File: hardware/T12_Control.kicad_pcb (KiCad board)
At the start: 2 copper layers, 33 parts, among them J1 Screw_Terminal_01x02, J3 Conn_01x07_Female, J4 Conn_01x04_Female, J5 Conn_01x06_Male, J6 Conn_01x04_Male, Q1 TPC8107, Q2 SI2308A, U1 LF15_TO252, U2 24LC32, U3 SGM8551XN, U4 STM32F103CBTx

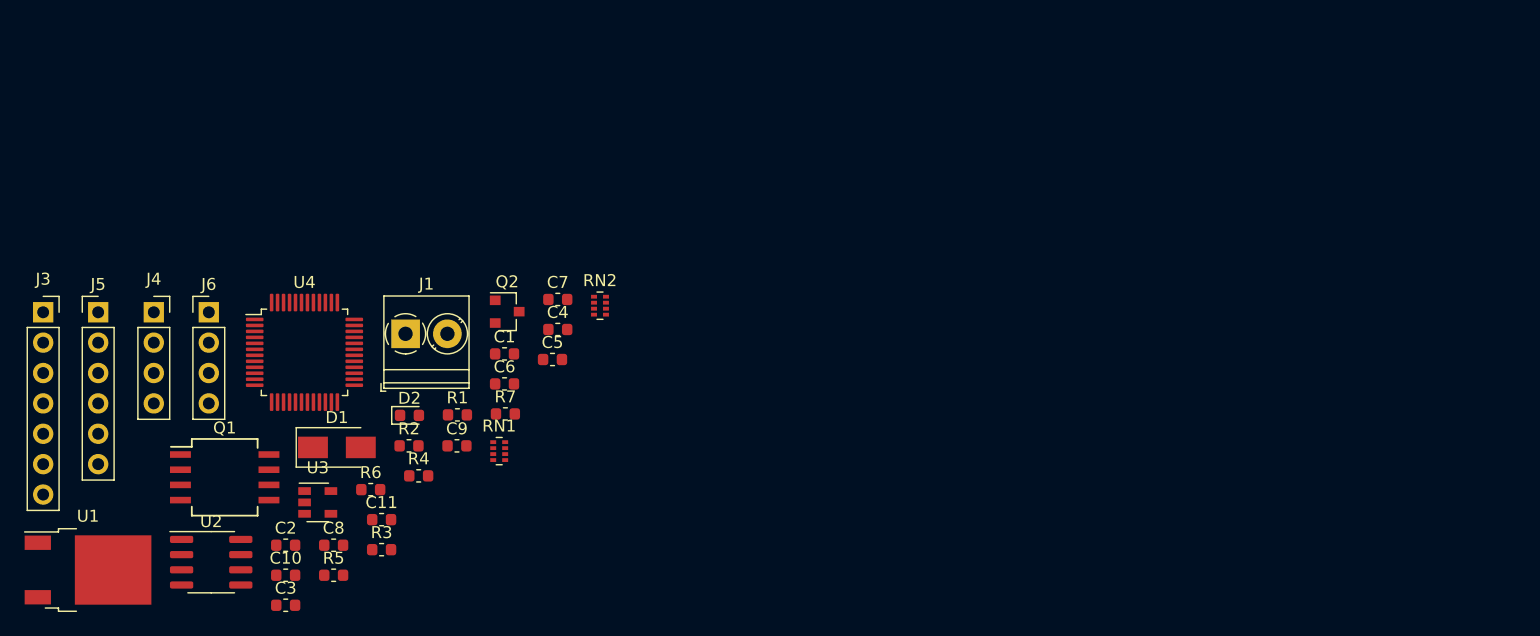
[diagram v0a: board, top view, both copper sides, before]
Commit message: Routhe the T12 Iron controller.
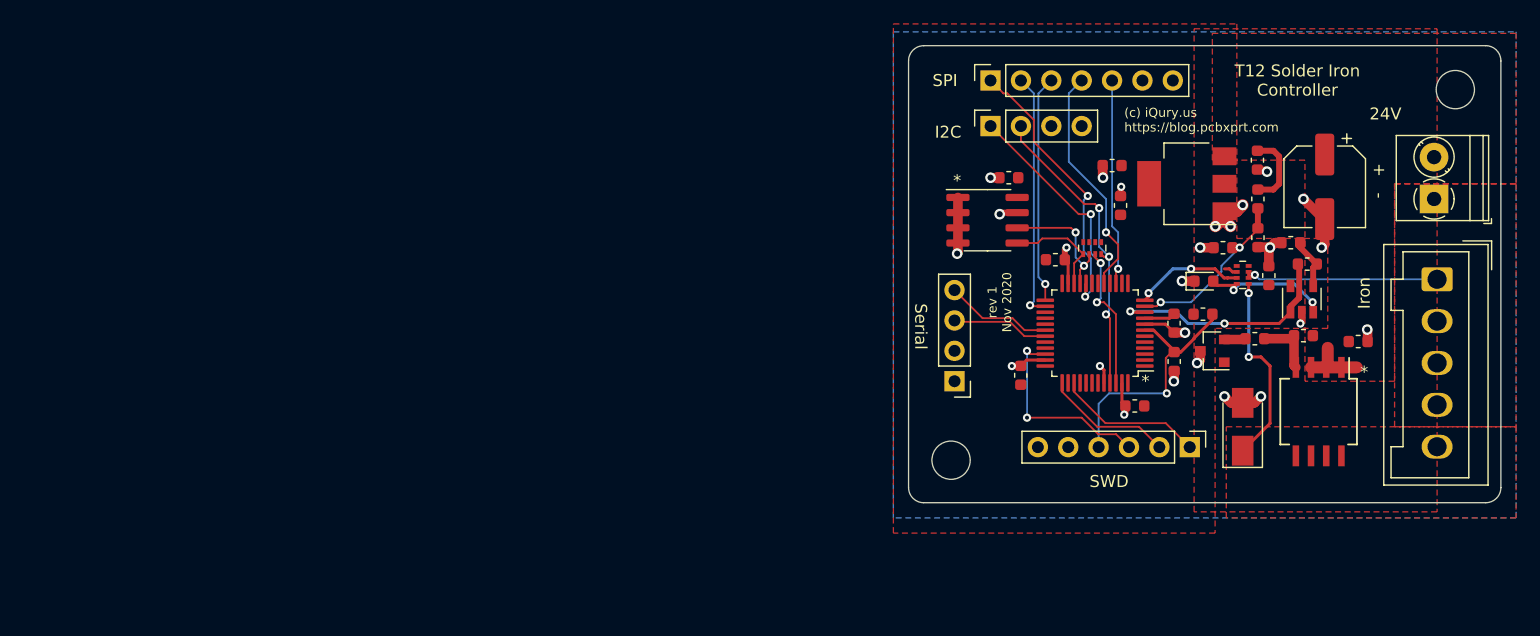
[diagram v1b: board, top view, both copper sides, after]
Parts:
- added C12: 100uF 35V, Capacitor_SMD:CP_Elec_6.3x7.7, F.Cu at (230.4, 82.8)
- added C13: 100nF, Capacitor_SMD:C_0603_1608Metric, F.Cu at (225.7, 90.2)
- added H1: MountingHole, MountingHole:MountingHole_3.2mm_M3_DIN965, F.Cu at (199.1, 105.7)
- added H2: MountingHole, MountingHole:MountingHole_3.2mm_M3_DIN965, F.Cu at (241.3, 74.7)
- added J2: GX12-5M, Connector_Wago:Wago_734-135_1x05_P3.50mm_Vertical, F.Cu at (239.8, 90.5)
- J3: value Conn_01x07_Female -> SPI LCD
- J4: value Conn_01x04_Female -> I2C LCD
- J5: value Conn_01x06_Male -> SWD
- J6: value Conn_01x04_Male -> Serial
- U1: value LF15_TO252 -> AMS1117-3.3; footprint Package_TO_SOT_SMD:TO-252-2 -> Package_TO_SOT_SMD:SOT-223-3_TabPin2
- moved U1 97.4 mm to (218.8, 82.5), turned to 180 degrees
- moved J5 92.0 mm to (219.1, 104.6), turned to -90 degrees
- moved Q1 91.6 mm to (229.9, 101.6), turned to -90 degrees
- moved C2 87.4 mm to (224.8, 80.6), turned to -90 degrees
- moved J1 86.7 mm to (239.5, 83.8), turned to 90 degrees
- moved R5 84.7 mm to (227.5, 87.5), turned to 180 degrees
- moved U3 84.0 mm to (228.5, 92.2), turned to 90 degrees
- moved J3 81.6 mm to (202.4, 73.9), turned to 90 degrees
- moved R6 80.6 mm to (228.9, 89.3), turned to 180 degrees
- moved C3 77.4 mm to (213.3, 84.4), turned to 90 degrees
- moved C10 77.2 mm to (217.8, 94.2), turned to -90 degrees
- moved D1 75.8 mm to (223.5, 102.9), turned to 90 degrees
- moved R3 75.1 mm to (224.5, 95.5), turned to 180 degrees
- moved R2 73.9 mm to (224.8, 83.8), turned to -90 degrees
- moved R4 72.9 mm to (224.8, 87.1), turned to -90 degrees
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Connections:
- Q2 pad 1: /HEARER_ON -> (no net)
- RN1 pad 1: Net-(RN1-Pad1) -> (no net)
- RN1 pad 8: Net-(RN1-Pad8) -> (no net)
- U1 pad 1: /24V -> GND
- U1 pad 2: GND -> /3.3V
- U1 pad 3: /3.3V -> /24V
- U4 pad 13: /ADC2 -> (no net)
- U4 pad 14: Net-(U4-Pad14) -> (no net)
- U4 pad 16: /MISO -> (no net)
- U4 pad 18: /PWM2 -> (no net)
- U4 pad 19: /PWM3 -> (no net)
- U4 pad 2: /IO_1 -> (no net)
- U4 pad 27: Net-(U4-Pad27) -> (no net)
- U4 pad 28: Net-(U4-Pad28) -> (no net)
- U4 pad 29: /HEATER_ON -> (no net)
- U4 pad 3: /IO_2 -> (no net)
- U4 pad 32: Net-(U4-Pad32) -> (no net)
- U4 pad 33: Net-(U4-Pad33) -> (no net)
- U4 pad 38: /PWM1 -> (no net)
- U4 pad 4: /IO_3 -> (no net)
- U4 pad 40: Net-(U4-Pad40) -> (no net)
- U4 pad 41: Net-(U4-Pad41) -> (no net)
- U4 pad 42: Net-(U4-Pad42) -> (no net)
- U4 pad 43: Net-(U4-Pad43) -> (no net)
- U4 pad 5: Net-(U4-Pad5) -> (no net)
- U4 pad 6: Net-(U4-Pad6) -> (no net)
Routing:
- net GND: track 0.00 -> 47.0 mm, vias 0 -> 25
- net /OLED_SDA: track 0.00 -> 28.0 mm, vias 0 -> 3
- net /OLED_SCL: track 0.00 -> 26.1 mm, vias 0 -> 3
- net /~CS: track 0.00 -> 23.4 mm, vias 0 -> 2
- net /~NRST: track 0.00 -> 21.7 mm, vias 0 -> 1
- net /D/~C: track 0.00 -> 20.7 mm, vias 0 -> 1
- net /TIP_TEMP: track 0.00 -> 19.8 mm, vias 0 -> 2
- net /MOSI: track 0.00 -> 19.6 mm, vias 0 -> 1
- net /~RST: track 0.00 -> 19.1 mm, vias 0 -> 1
- net /SCK: track 0.00 -> 17.2 mm, vias 0 -> 1
- net /SWDIO: track 0.00 -> 16.8 mm, vias 0 -> 2
- net Net-(J2-Pad1): track 0.00 -> 16.5 mm, vias 0 -> 1
- net Net-(D1-Pad1): track 0.00 -> 16.2 mm, vias 0 -> 2
- net /V_MON: track 0.00 -> 14.8 mm, vias 0 -> 2
- net /SWDSWO: track 0.00 -> 12.3 mm
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- added copper zone on F.Cu, net /24V
- added copper zone on F.Cu, net /3.3V
- added copper zone on B.Cu, net GND
- added copper zone on F.Cu, net GND
- added copper zone on F.Cu, net Net-(D1-Pad1)
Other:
- board outline added: 49.5 x 38.2 mm
- board text added: "(c) iQury.us https://blog.pcbxprt.com"
- board text added: "*"
- board text added: "+ -"
- board text added: "24V"
- board text added: "3.3V"
- board text added: "D/~C"
- board text added: "GND"
- board text added: "HEATER"
- board text added: "I2C"
- board text added: "Iron"
- board text added: "MOSI"
- board text added: "N/C"
- board text added: "NTC"
- board text added: "RX"
- board text added: "SCK"
- board text added: "SCL"
- board text added: "SDA"
- board text added: "SPI"
- board text added: "SWD"
- board text added: "SWDCLK"
- board text added: "SWDIO"
- board text added: "SWDSWO"
- board text added: "Serial"
- board text added: "T12 Solder Iron Controller"
- board text added: "TX"
- board text added: "rev 1 Nov 2020"
- board text added: "~CS"
- board text added: "~RESET"
- board text added: "~RST"

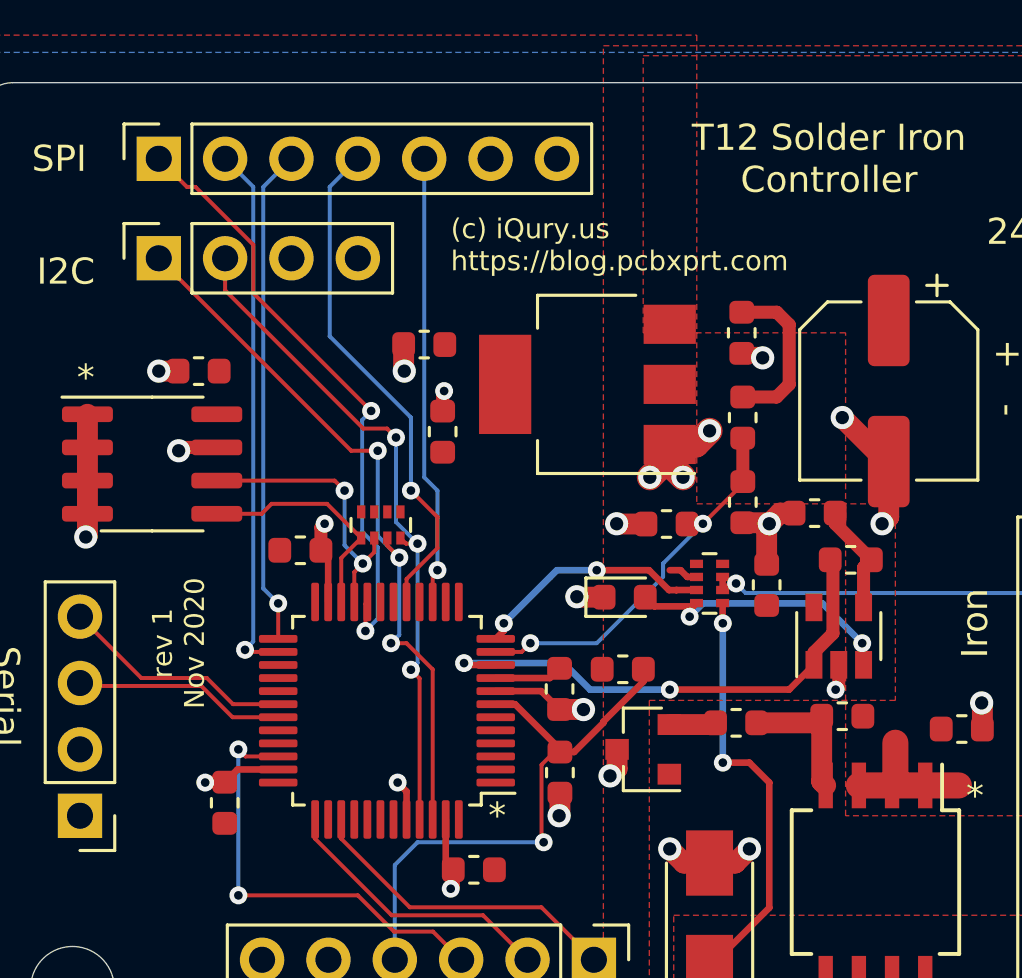
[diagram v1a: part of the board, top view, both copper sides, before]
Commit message: Added LCSC Part #s Generated fab files.
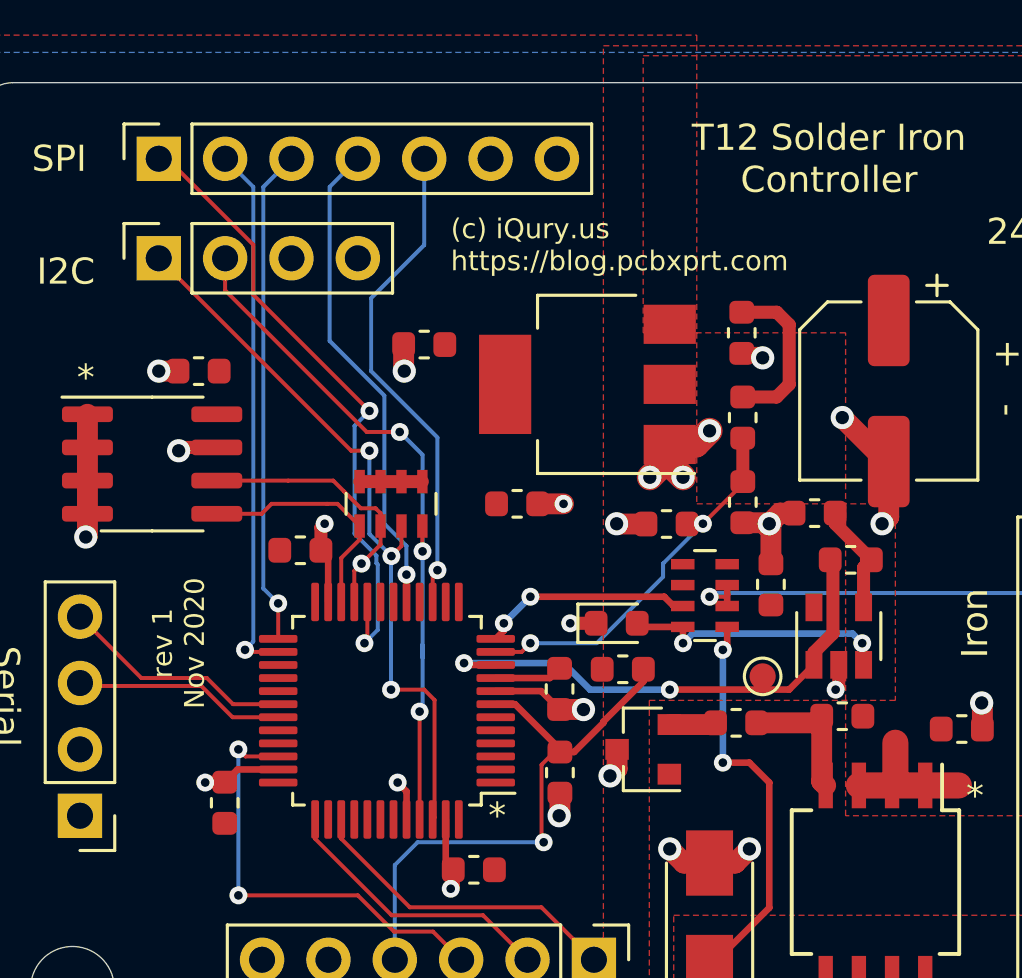
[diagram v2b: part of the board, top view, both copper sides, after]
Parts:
- added TP1: TestPoint, TestPoint:TestPoint_Pad_D1.0mm, F.Cu at (225.6, 93.7)
- C5: value 6.3uF -> 10uF
- RN1, RN2: footprint Resistor_SMD:R_Array_Concave_4x0402 -> Resistor_SMD:R_Array_Concave_4x0603
- moved C3 3.97 mm to (216.2, 87.1), turned to 0 degrees
- moved D2 1.04 mm to (220.0, 91.7)
- moved RN2 0.90 mm to (211.3, 87.1)
- moved RN1 0.49 mm to (223.3, 90.6)
- moved C13 0.16 mm to (225.9, 90.2)
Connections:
- RN1 pad 1: (no net) -> Net-(RN1-Pad1)
- RN1 pad 8: (no net) -> Net-(RN1-Pad8)
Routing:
- net /SCK: track 17.2 -> 18.9 mm
- net Net-(J2-Pad1): track 16.5 -> 17.8 mm
- net /3.3V: track 3.73 -> 5.00 mm
- net /~CS: track 23.4 -> 24.5 mm
- net /NTC: track 9.26 -> 8.14 mm
- net /MOSI: track 19.6 -> 18.6 mm
- net Net-(D1-Pad1): track 16.2 -> 15.4 mm
- net /OLED_SCL: track 26.1 -> 26.9 mm
- net Net-(D2-Pad2): track 11.1 -> 10.4 mm
- net /EE_SCL: track 11.1 -> 10.6 mm, vias 2 -> 1

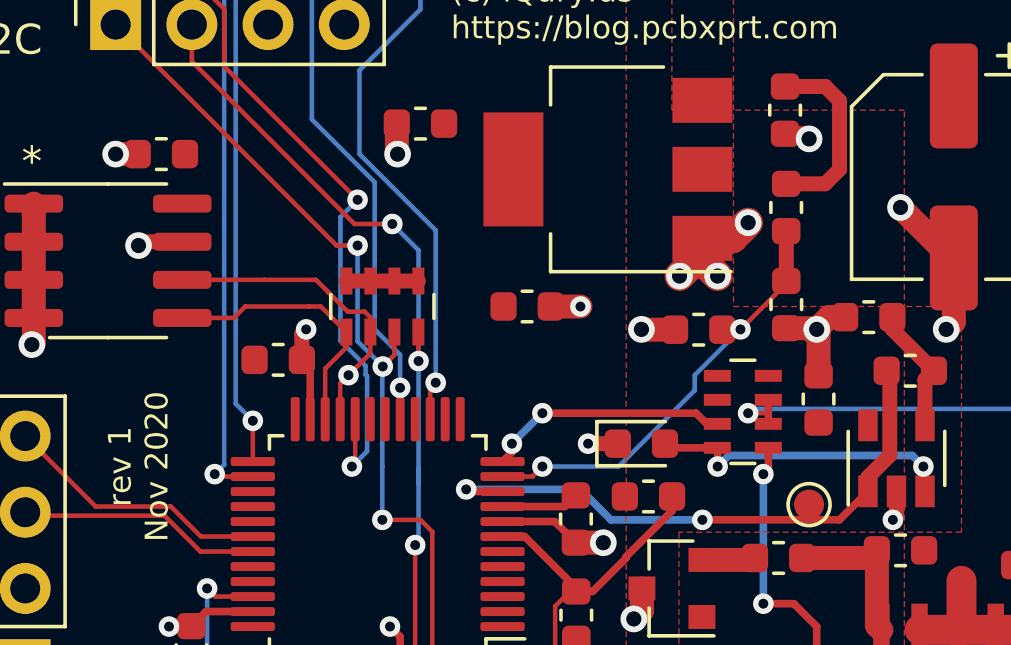
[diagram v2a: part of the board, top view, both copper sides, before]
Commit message: Revert the resistor networks back to 4x0402 footprint, not using JLC assembly svc for now.
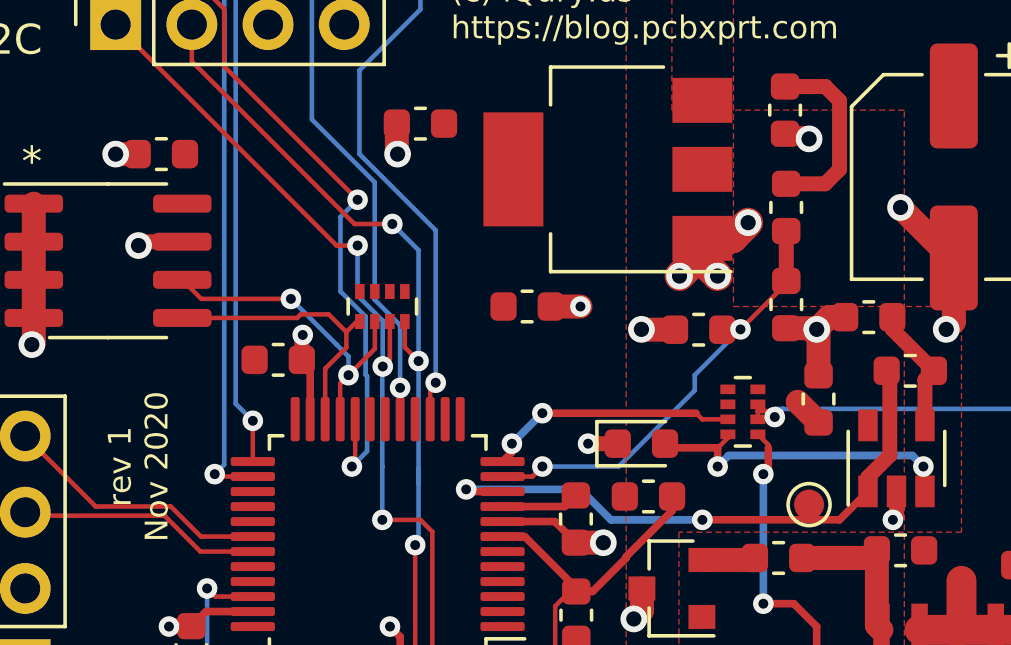
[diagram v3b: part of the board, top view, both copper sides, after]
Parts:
- RN1, RN2: footprint Resistor_SMD:R_Array_Concave_4x0603 -> Resistor_SMD:R_Array_Concave_4x0402
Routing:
- net /3.3V: track 5.00 -> 3.58 mm
- net Net-(J2-Pad1): track 17.8 -> 16.9 mm
- net Net-(D2-Pad2): track 10.4 -> 11.0 mm
- net Net-(D1-Pad1): track 15.4 -> 16.0 mm
- net /OLED_SCL: track 26.9 -> 27.4 mm
- net /EE_SCL: track 10.6 -> 11.0 mm, vias 1 -> 2

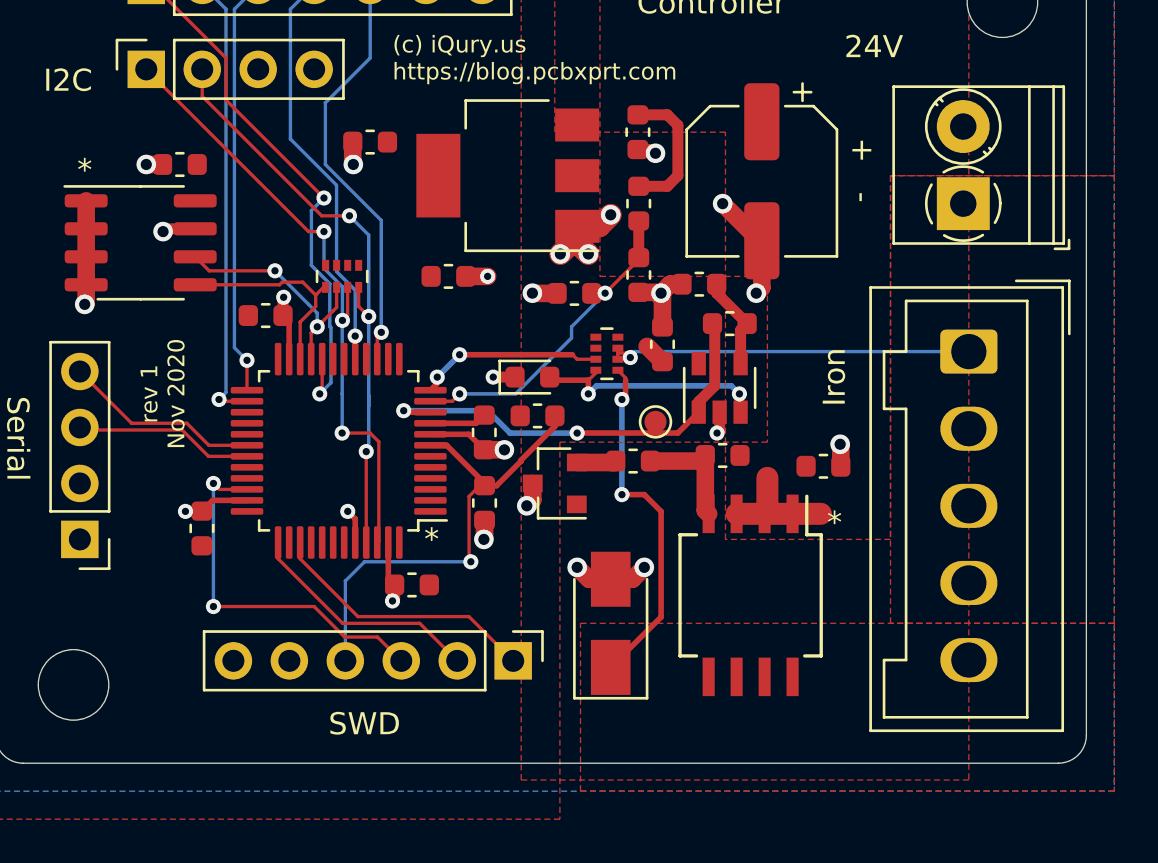
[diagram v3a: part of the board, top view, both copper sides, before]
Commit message: Update the 1N4148 diodes to B5819W. The 1N was too puny to serve as protection.
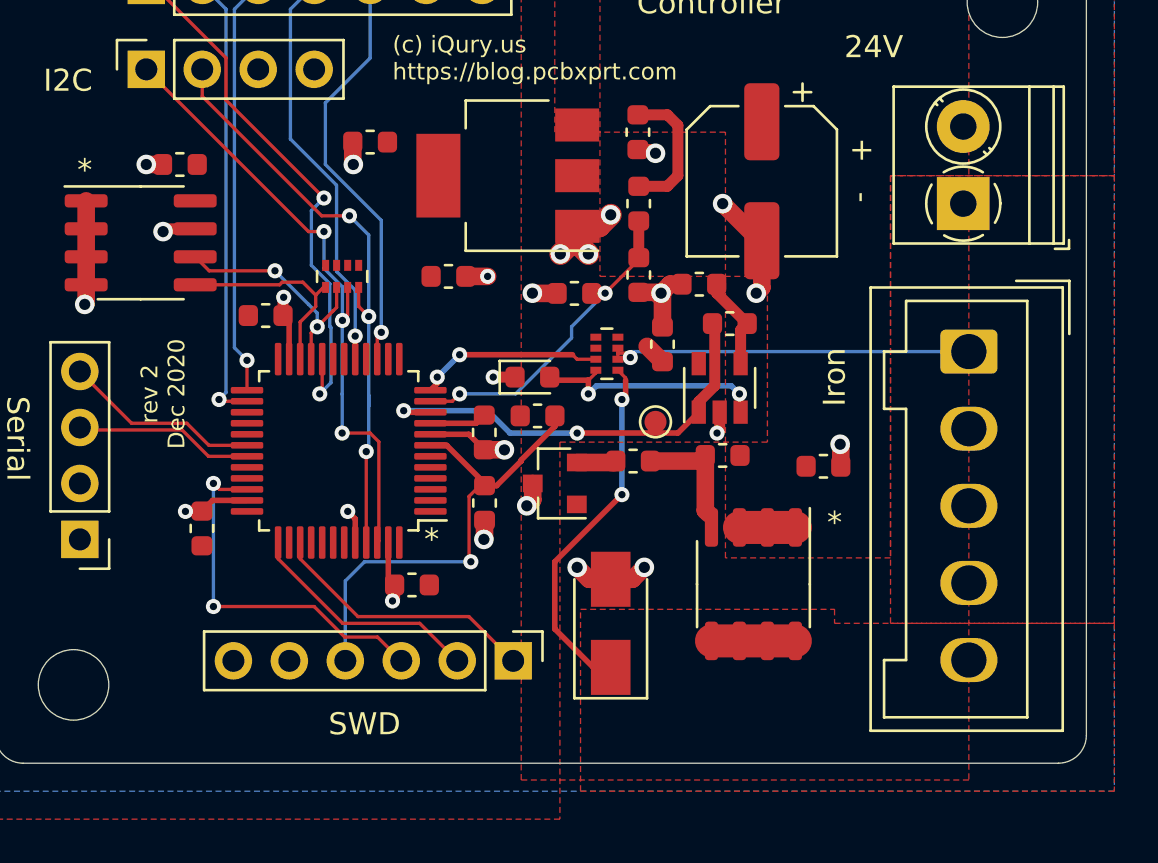
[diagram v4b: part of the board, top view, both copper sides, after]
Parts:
- Q1: footprint Package_SO:SO-8_5.3x6.2mm_P1.27mm -> Package_SO:SO-8_3.9x4.9mm_P1.27mm
- moved Q1 0.52 mm to (230.0, 101.1)
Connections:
- RN1 pad 1: Net-(RN1-Pad1) -> (no net)
- RN1 pad 8: Net-(RN1-Pad8) -> (no net)
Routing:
- net Net-(D1-Pad1): track 16.0 -> 20.3 mm
- net /24V: track 11.8 -> 8.82 mm
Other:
- board text added: "rev 2 Dec 2020"
- board text removed: "rev 1 Nov 2020"
